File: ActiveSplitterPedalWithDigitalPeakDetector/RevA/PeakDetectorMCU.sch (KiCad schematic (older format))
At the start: 22 parts, among them J7 Conn_01x05, U4 STM32F051K8Tx

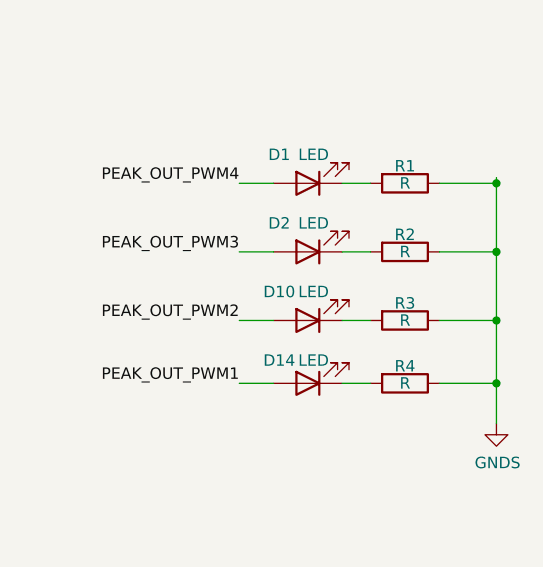
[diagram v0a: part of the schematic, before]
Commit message: hw update
moved led resistors to back copper layer
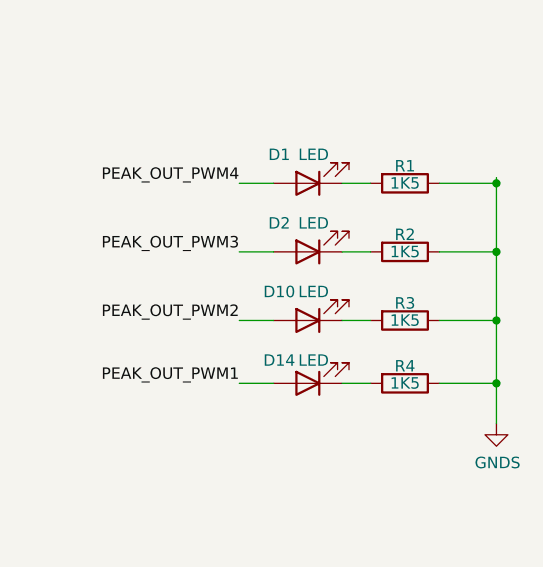
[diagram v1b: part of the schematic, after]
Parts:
- R1, R2, R3, R4: value R -> 1K5
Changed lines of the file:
@@
 P 10025 3175
 F 0 "R4" V 9950 3175 50  0000 C CNN
-F 1 "R" V 10025 3175 50  0000 C CNN
+F 1 "1K5" V 10025 3175 50  0000 C CNN
 F 2 "Resistor_SMD:R_0805_2012Metric_Pad1.15x1.40mm_HandSolder" V 9955 3175 50  0001 C CNN
 F 3 "~" H 10025 3175 50  0001 C CNN
@@
 P 10025 2900
 F 0 "R3" V 9950 2900 50  0000 C CNN
-F 1 "R" V 10025 2900 50  0000 C CNN
+F 1 "1K5" V 10025 2900 50  0000 C CNN
 F 2 "Resistor_SMD:R_0805_2012Metric_Pad1.15x1.40mm_HandSolder" V 9955 2900 50  0001 C CNN
 F 3 "~" H 10025 2900 50  0001 C CNN
@@
 P 10025 2600
 F 0 "R2" V 9950 2600 50  0000 C CNN
-F 1 "R" V 10025 2600 50  0000 C CNN
+F 1 "1K5" V 10025 2600 50  0000 C CNN
 F 2 "Resistor_SMD:R_0805_2012Metric_Pad1.15x1.40mm_HandSolder" V 9955 2600 50  0001 C CNN
 F 3 "~" H 10025 2600 50  0001 C CNN
@@
 P 10025 2300
 F 0 "R1" V 9950 2300 50  0000 C CNN
-F 1 "R" V 10025 2300 50  0000 C CNN
+F 1 "1K5" V 10025 2300 50  0000 C CNN
 F 2 "Resistor_SMD:R_0805_2012Metric_Pad1.15x1.40mm_HandSolder" V 9955 2300 50  0001 C CNN
 F 3 "~" H 10025 2300 50  0001 C CNN
